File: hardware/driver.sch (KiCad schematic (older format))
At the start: 12 parts

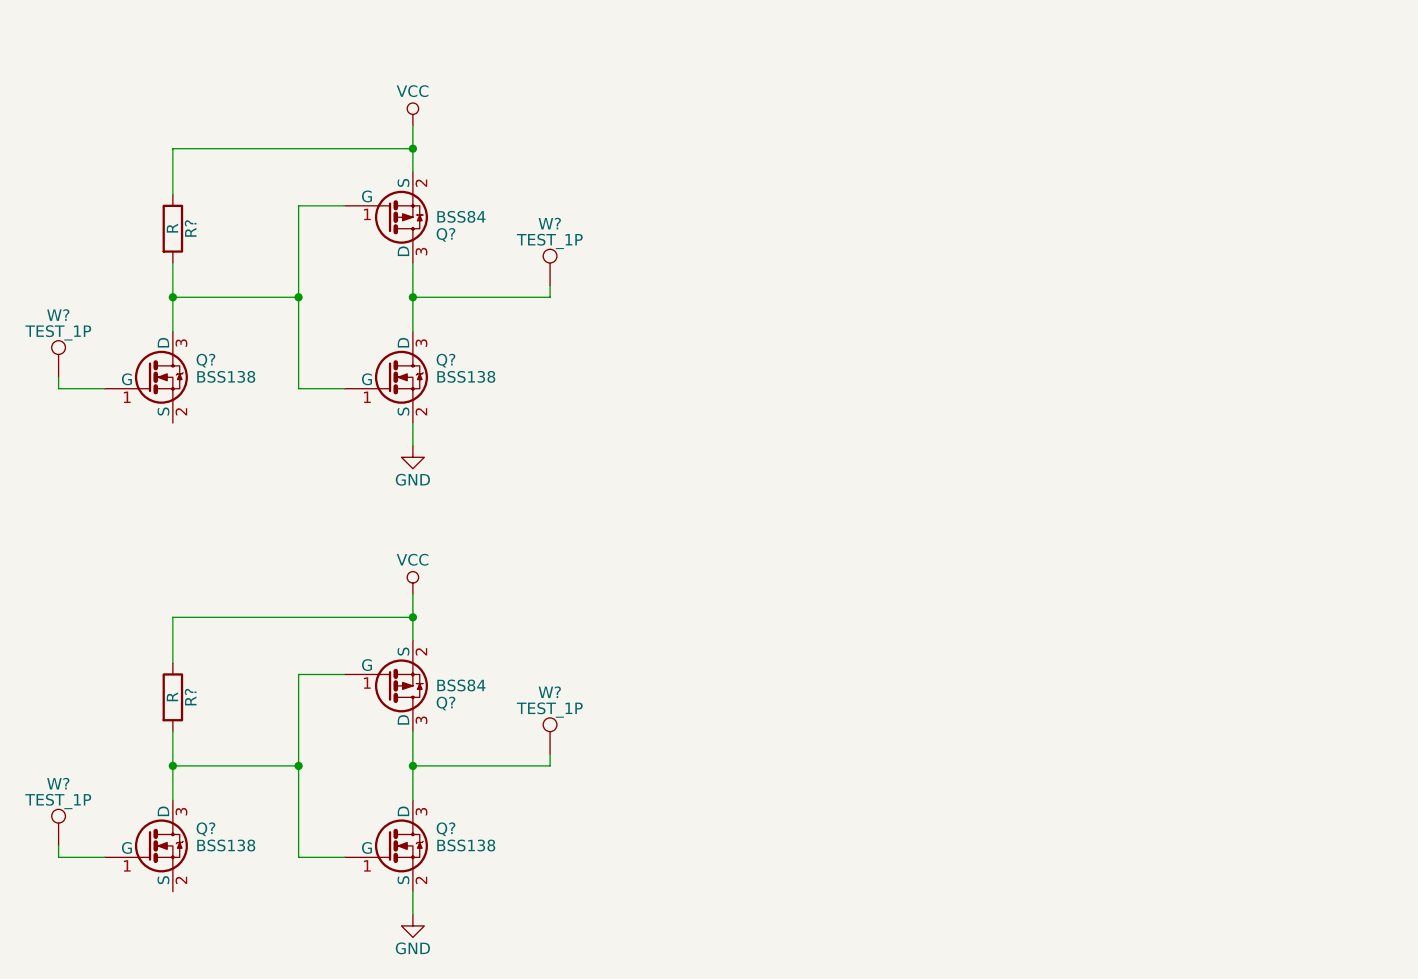
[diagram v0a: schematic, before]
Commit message: Fixed FET orientation
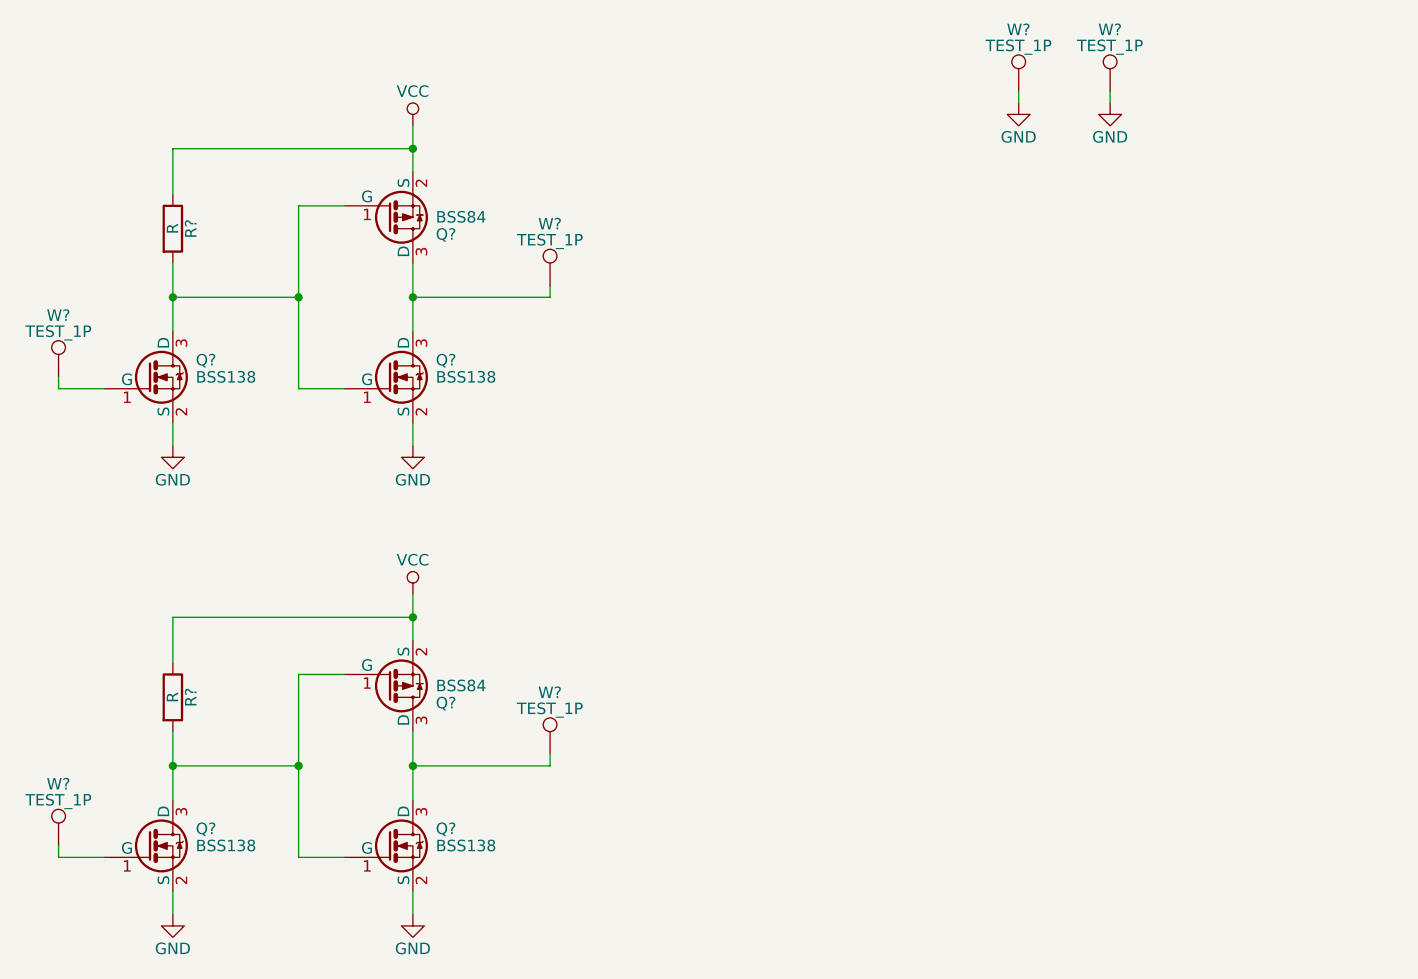
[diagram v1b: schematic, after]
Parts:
- added W? (x2): TEST_1P, symbol TEST_1P
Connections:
- net GND: now also Q?.2 (S), Q?.2 (S), W?.1, W?.1
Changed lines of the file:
@@
 	3500 3850 3500 4050
 Connection ~ 4550 3850
+$Comp
+L GND #PWR?
+U 1 1 5890FAB7
+P 3500 3100
+F 0 "#PWR?" H 3500 2850 50  0001 C CNN
+F 1 "GND" H 3500 2950 50  0000 C CNN
+F 2 "" H 3500 3100 50  0000 C CNN
+F 3 "" H 3500 3100 50  0000 C CNN
+	1    3500 3100
+	1    0    0    -1
+$EndComp
+Wire Wire Line
+	3500 3100 3500 3000
+$Comp
+L GND #PWR?
+U 1 1 5890FD28
+P 3500 5150
+F 0 "#PWR?" H 3500 4900 50  0001 C CNN
+F 1 "GND" H 3500 5000 50  0000 C CNN
+F 2 "" H 3500 5150 50  0000 C CNN
+F 3 "" H 3500 5150 50  0000 C CNN
+	1    3500 5150
+	1    0    0    -1
+$EndComp
+Wire Wire Line
+	3500 5150 3500 5050
+$Comp
+L TEST_1P W?
+U 1 1 58910040
+P 7200 1550
+F 0 "W?" H 7200 1820 50  0000 C CNN
+F 1 "TEST_1P" H 7200 1750 50  0000 C CNN
+F 2 "" H 7400 1550 50  0000 C CNN
+F 3 "" H 7400 1550 50  0000 C CNN
+	1    7200 1550
+	1    0    0    -1
+$EndComp
+$Comp
+L TEST_1P W?
+U 1 1 58910461
+P 7600 1550
+F 0 "W?" H 7600 1820 50  0000 C CNN
+F 1 "TEST_1P" H 7600 1750 50  0000 C CNN
+F 2 "" H 7800 1550 50  0000 C CNN
+F 3 "" H 7800 1550 50  0000 C CNN
+	1    7600 1550
+	1    0    0    -1
+$EndComp
+$Comp
+L GND #PWR?
+U 1 1 5891056F
+P 7200 1600
+F 0 "#PWR?" H 7200 1350 50  0001 C CNN
+F 1 "GND" H 7200 1450 50  0000 C CNN
+F 2 "" H 7200 1600 50  0000 C CNN
+F 3 "" H 7200 1600 50  0000 C CNN
+	1    7200 1600
+	1    0    0    -1
+$EndComp
+$Comp
+L GND #PWR?
+U 1 1 589105A4
+P 7600 1600
+F 0 "#PWR?" H 7600 1350 50  0001 C CNN
+F 1 "GND" H 7600 1450 50  0000 C CNN
+F 2 "" H 7600 1600 50  0000 C CNN
+F 3 "" H 7600 1600 50  0000 C CNN
+	1    7600 1600
+	1    0    0    -1
+$EndComp
+Wire Wire Line
+	7600 1600 7600 1550
+Wire Wire Line
+	7200 1550 7200 1600
 $EndSCHEMATC

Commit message: Added power flags
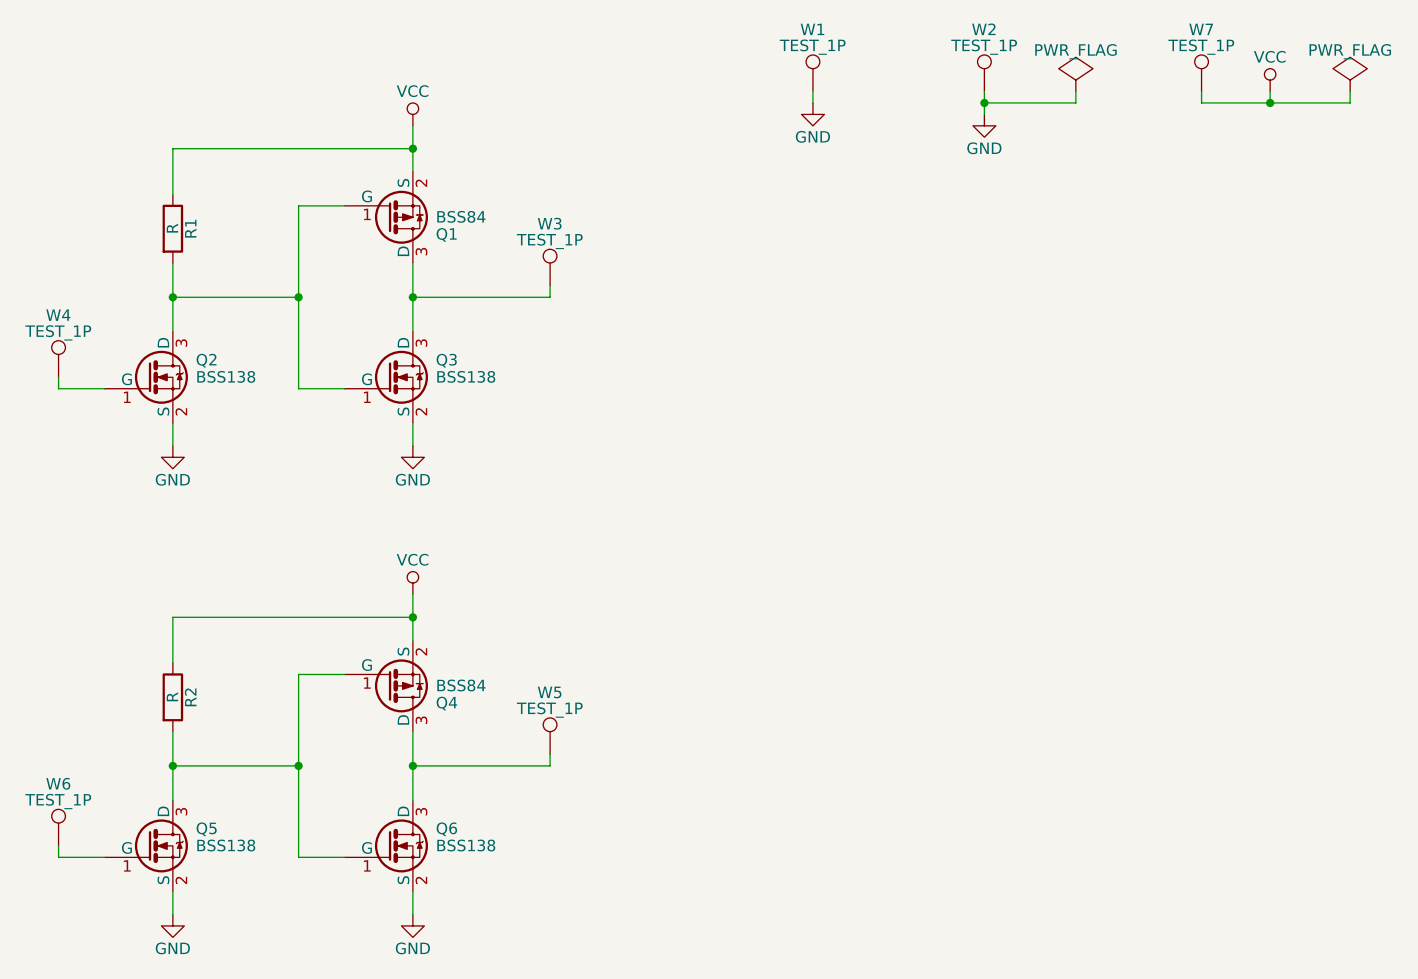
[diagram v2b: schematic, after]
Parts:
- added W7: TEST_1P, symbol TEST_1P
- gave numbers to parts that had none: 14
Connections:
- net VCC: now also W7.1
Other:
- moved on the sheet: W1, W2
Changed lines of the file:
@@
 $EndDescr
 $Comp
-L BSS84 Q?
+L BSS84 Q1
 U 1 1 588FBBAA
 P 4450 2100
-F 0 "Q?" H 4650 2175 50  0000 L CNN
+F 0 "Q1" H 4650 2175 50  0000 L CNN
 F 1 "BSS84" H 4650 2100 50  0000 L CNN
 F 2 "" H 4650 2025 50  0000 L CIN
@@
 $EndComp
 $Comp
-L BSS138 Q?
+L BSS138 Q2
 U 1 1 588FBC23
 P 3400 2800
-F 0 "Q?" H 3600 2875 50  0000 L CNN
+F 0 "Q2" H 3600 2875 50  0000 L CNN
 F 1 "BSS138" H 3600 2800 50  0000 L CNN
 F 2 "TO_SOT_Packages_SMD:SOT-23" H 3600 2725 50  0001 L CIN
@@
 $EndComp
 $Comp
-L GND #PWR?
+L GND #PWR01
 U 1 1 588FBD14
 P 4550 3100
-F 0 "#PWR?" H 4550 2850 50  0001 C CNN
+F 0 "#PWR01" H 4550 2850 50  0001 C CNN
 F 1 "GND" H 4550 2950 50  0000 C CNN
 F 2 "" H 4550 3100 50  0000 C CNN
@@
 $EndComp
 $Comp
-L VCC #PWR?
+L VCC #PWR02
 U 1 1 588FBD2C
 P 4550 1700
-F 0 "#PWR?" H 4550 1550 50  0001 C CNN
+F 0 "#PWR02" H 4550 1550 50  0001 C CNN
 F 1 "VCC" H 4550 1850 50  0000 C CNN
 F 2 "" H 4550 1700 50  0000 C CNN
@@
 $EndComp
 $Comp
-L R R?
+L R R1
 U 1 1 588FBD46
 P 3500 2150
-F 0 "R?" V 3580 2150 50  0000 C CNN
+F 0 "R1" V 3580 2150 50  0000 C CNN
 F 1 "R" V 3500 2150 50  0000 C CNN
 F 2 "" V 3430 2150 50  0000 C CNN
@@
 $EndComp
 $Comp
-L TEST_1P W?
+L TEST_1P W4
 U 1 1 588FBD89
 P 3000 2800
-F 0 "W?" H 3000 3070 50  0000 C CNN
+F 0 "W4" H 3000 3070 50  0000 C CNN
 F 1 "TEST_1P" H 3000 3000 50  0000 C CNN
 F 2 "" H 3200 2800 50  0000 C CNN
@@
 $EndComp
 $Comp
-L BSS138 Q?
+L BSS138 Q3
 U 1 1 588FC012
 P 4450 2800
-F 0 "Q?" H 4650 2875 50  0000 L CNN
+F 0 "Q3" H 4650 2875 50  0000 L CNN
 F 1 "BSS138" H 4650 2800 50  0000 L CNN
 F 2 "TO_SOT_Packages_SMD:SOT-23" H 4650 2725 50  0001 L CIN
@@
 	4550 3100 4550 3000
 $Comp
-L VCC #PWR?
+L VCC #PWR03
 U 1 1 588FC3B7
 P 4550 3750
-F 0 "#PWR?" H 4550 3600 50  0001 C CNN
+F 0 "#PWR03" H 4550 3600 50  0001 C CNN
 F 1 "VCC" H 4550 3900 50  0000 C CNN
 F 2 "" H 4550 3750 50  0000 C CNN
@@
 $EndComp
 $Comp
-L BSS84 Q?
+L BSS84 Q4
 U 1 1 588FC42B
 P 4450 4150
-F 0 "Q?" H 4650 4225 50  0000 L CNN
+F 0 "Q4" H 4650 4225 50  0000 L CNN
 F 1 "BSS84" H 4650 4150 50  0000 L CNN
 F 2 "" H 4650 4075 50  0000 L CIN
@@
 Connection ~ 4550 4500
 $Comp
-L BSS138 Q?
+L BSS138 Q6
 U 1 1 588FC62C
 P 4450 4850
-F 0 "Q?" H 4650 4925 50  0000 L CNN
+F 0 "Q6" H 4650 4925 50  0000 L CNN
 F 1 "BSS138" H 4650 4850 50  0000 L CNN
 F 2 "TO_SOT_Packages_SMD:SOT-23" H 4650 4775 50  0001 L CIN
@@
 $EndComp
 $Comp
-L GND #PWR?
+L GND #PWR04
 U 1 1 588FC66D
 P 4550 5150
-F 0 "#PWR?" H 4550 4900 50  0001 C CNN
+F 0 "#PWR04" H 4550 4900 50  0001 C CNN
 F 1 "GND" H 4550 5000 50  0000 C CNN
 F 2 "" H 4550 5150 50  0000 C CNN
@@
 Connection ~ 4050 4500
 $Comp
-L BSS138 Q?
+L BSS138 Q5
 U 1 1 588FC9C8
 P 3400 4850
-F 0 "Q?" H 3600 4925 50  0000 L CNN
+F 0 "Q5" H 3600 4925 50  0000 L CNN
 F 1 "BSS138" H 3600 4850 50  0000 L CNN
 F 2 "TO_SOT_Packages_SMD:SOT-23" H 3600 4775 50  0001 L CIN
@@
 Connection ~ 3500 4500
 $Comp
-L R R?
+L R R2
 U 1 1 588FCB0A
 P 3500 4200
-F 0 "R?" V 3580 4200 50  0000 C CNN
+F 0 "R2" V 3580 4200 50  0000 C CNN
 F 1 "R" V 3500 4200 50  0000 C CNN
 F 2 "" V 3430 4200 50  0000 C CNN
@@
 	3000 2850 3000 2800
 $Comp
-L TEST_1P W?
+L TEST_1P W6
 U 1 1 588FCDEE
 P 3000 4850
-F 0 "W?" H 3000 5120 50  0000 C CNN
+F 0 "W6" H 3000 5120 50  0000 C CNN
 F 1 "TEST_1P" H 3000 5050 50  0000 C CNN
 F 2 "" H 3200 4850 50  0000 C CNN
@@
 	3000 4900 3000 4850
 $Comp
-L TEST_1P W?
+L TEST_1P W5
 U 1 1 588FD19C
 P 5150 4450
-F 0 "W?" H 5150 4720 50  0000 C CNN
+F 0 "W5" H 5150 4720 50  0000 C CNN
 F 1 "TEST_1P" H 5150 4650 50  0000 C CNN
 F 2 "" H 5350 4450 50  0000 C CNN
@@
 $EndComp
 $Comp
-L TEST_1P W?
+L TEST_1P W3
 U 1 1 588FD262
 P 5150 2400
-F 0 "W?" H 5150 2670 50  0000 C CNN
+F 0 "W3" H 5150 2670 50  0000 C CNN
 F 1 "TEST_1P" H 5150 2600 50  0000 C CNN
 F 2 "" H 5350 2400 50  0000 C CNN
@@
 Connection ~ 4550 3850
 $Comp
-L GND #PWR?
+L GND #PWR05
 U 1 1 5890FAB7
 P 3500 3100
-F 0 "#PWR?" H 3500 2850 50  0001 C CNN
+F 0 "#PWR05" H 3500 2850 50  0001 C CNN
 F 1 "GND" H 3500 2950 50  0000 C CNN
 F 2 "" H 3500 3100 50  0000 C CNN
@@
 	3500 3100 3500 3000
 $Comp
-L GND #PWR?
+L GND #PWR06
 U 1 1 5890FD28
 P 3500 5150
-F 0 "#PWR?" H 3500 4900 50  0001 C CNN
+F 0 "#PWR06" H 3500 4900 50  0001 C CNN
 F 1 "GND" H 3500 5000 50  0000 C CNN
 F 2 "" H 3500 5150 50  0000 C CNN
@@
 	3500 5150 3500 5050
 $Comp
-L TEST_1P W?
+L TEST_1P W1
 U 1 1 58910040
-P 7200 1550
-F 0 "W?" H 7200 1820 50  0000 C CNN
-F 1 "TEST_1P" H 7200 1750 50  0000 C CNN
-F 2 "" H 7400 1550 50  0000 C CNN
-F 3 "" H 7400 1550 50  0000 C CNN
-	1    7200 1550
-	1    0    0    -1
-$EndComp
-$Comp
-L TEST_1P W?
+P 6300 1550
+F 0 "W1" H 6300 1820 50  0000 C CNN
+F 1 "TEST_1P" H 6300 1750 50  0000 C CNN
+F 2 "" H 6500 1550 50  0000 C CNN
+F 3 "" H 6500 1550 50  0000 C CNN
+	1    6300 1550
+	1    0    0    -1
+$EndComp
+$Comp
+L TEST_1P W2
 U 1 1 58910461
-P 7600 1550
-F 0 "W?" H 7600 1820 50  0000 C CNN
-F 1 "TEST_1P" H 7600 1750 50  0000 C CNN
-F 2 "" H 7800 1550 50  0000 C CNN
-F 3 "" H 7800 1550 50  0000 C CNN
-	1    7600 1550
-	1    0    0    -1
-$EndComp
-$Comp
-L GND #PWR?
+P 7050 1550
+F 0 "W2" H 7050 1820 50  0000 C CNN
+F 1 "TEST_1P" H 7050 1750 50  0000 C CNN
+F 2 "" H 7250 1550 50  0000 C CNN
+F 3 "" H 7250 1550 50  0000 C CNN
+	1    7050 1550
+	1    0    0    -1
+$EndComp
+$Comp
+L GND #PWR07
 U 1 1 5891056F
-P 7200 1600
-F 0 "#PWR?" H 7200 1350 50  0001 C CNN
-F 1 "GND" H 7200 1450 50  0000 C CNN
-F 2 "" H 7200 1600 50  0000 C CNN
-F 3 "" H 7200 1600 50  0000 C CNN
-	1    7200 1600
-	1    0    0    -1
-$EndComp
-$Comp
-L GND #PWR?
+P 6300 1600
+F 0 "#PWR07" H 6300 1350 50  0001 C CNN
+F 1 "GND" H 6300 1450 50  0000 C CNN
+F 2 "" H 6300 1600 50  0000 C CNN
+F 3 "" H 6300 1600 50  0000 C CNN
+	1    6300 1600
+	1    0    0    -1
+$EndComp
+$Comp
+L GND #PWR08
 U 1 1 589105A4
-P 7600 1600
-F 0 "#PWR?" H 7600 1350 50  0001 C CNN
-F 1 "GND" H 7600 1450 50  0000 C CNN
-F 2 "" H 7600 1600 50  0000 C CNN
-F 3 "" H 7600 1600 50  0000 C CNN
-	1    7600 1600
-	1    0    0    -1
-$EndComp
-Wire Wire Line
-	7600 1600 7600 1550
-Wire Wire Line
-	7200 1550 7200 1600
+P 7050 1650
+F 0 "#PWR08" H 7050 1400 50  0001 C CNN
+F 1 "GND" H 7050 1500 50  0000 C CNN
+F 2 "" H 7050 1650 50  0000 C CNN
+F 3 "" H 7050 1650 50  0000 C CNN
+	1    7050 1650
+	1    0    0    -1
+$EndComp
+Wire Wire Line
+	7050 1550 7050 1650
+Wire Wire Line
+	6300 1550 6300 1600
+$Comp
+L TEST_1P W7
+U 1 1 58922E12
+P 8000 1550
+F 0 "W7" H 8000 1820 50  0000 C CNN
+F 1 "TEST_1P" H 8000 1750 50  0000 C CNN
+F 2 "" H 8200 1550 50  0000 C CNN
+F 3 "" H 8200 1550 50  0000 C CNN
+	1    8000 1550
+	1    0    0    -1
+$EndComp
+$Comp
+L VCC #PWR09
+U 1 1 58922E63
+P 8300 1550
+F 0 "#PWR09" H 8300 1400 50  0001 C CNN
+F 1 "VCC" H 8300 1700 50  0000 C CNN
+F 2 "" H 8300 1550 50  0000 C CNN
+F 3 "" H 8300 1550 50  0000 C CNN
+	1    8300 1550
+	1    0    0    -1
+$EndComp
+Wire Wire Line
+	8000 1550 8000 1600
+Wire Wire Line
+	8000 1600 8650 1600
+Wire Wire Line
+	8300 1600 8300 1550
+$Comp
+L PWR_FLAG #FLG010
+U 1 1 5892349D
+P 8650 1550
+F 0 "#FLG010" H 8650 1645 50  0001 C CNN
+F 1 "PWR_FLAG" H 8650 1730 50  0000 C CNN
+F 2 "" H 8650 1550 50  0000 C CNN
+F 3 "" H 8650 1550 50  0000 C CNN
+	1    8650 1550
+	1    0    0    -1
+$EndComp
+Wire Wire Line
+	8650 1600 8650 1550
+Connection ~ 8300 1600
+$Comp
+L PWR_FLAG #FLG011
+U 1 1 589242AB
+P 7450 1550
+F 0 "#FLG011" H 7450 1645 50  0001 C CNN
+F 1 "PWR_FLAG" H 7450 1730 50  0000 C CNN
+F 2 "" H 7450 1550 50  0000 C CNN
+F 3 "" H 7450 1550 50  0000 C CNN
+	1    7450 1550
+	1    0    0    -1
+$EndComp
+Wire Wire Line
+	7050 1600 7450 1600
+Wire Wire Line
+	7450 1600 7450 1550
+Connection ~ 7050 1600
 $EndSCHEMATC

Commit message: Names/annotation
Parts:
- W2: value TEST_1P -> GND
- W3: value TEST_1P -> OUT1
- W4: value TEST_1P -> IN1
- W5: value TEST_1P -> OUT2
- W6: value TEST_1P -> IN2
- W7: value TEST_1P -> VCC
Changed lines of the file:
@@
 encoding utf-8
 Sheet 1 1
-Title ""
-Date ""
-Rev ""
-Comp ""
+Title "FET push-pull driver"
+Date "2017-02-01"
+Rev "1.0"
+Comp "KEIO"
 Comment1 ""
 Comment2 ""
@@
 P 3000 2800
 F 0 "W4" H 3000 3070 50  0000 C CNN
-F 1 "TEST_1P" H 3000 3000 50  0000 C CNN
+F 1 "IN1" H 3000 3000 50  0000 C CNN
 F 2 "" H 3200 2800 50  0000 C CNN
 F 3 "" H 3200 2800 50  0000 C CNN
@@
 P 3000 4850
 F 0 "W6" H 3000 5120 50  0000 C CNN
-F 1 "TEST_1P" H 3000 5050 50  0000 C CNN
+F 1 "IN2" H 3000 5050 50  0000 C CNN
 F 2 "" H 3200 4850 50  0000 C CNN
 F 3 "" H 3200 4850 50  0000 C CNN
@@
 P 5150 4450
 F 0 "W5" H 5150 4720 50  0000 C CNN
-F 1 "TEST_1P" H 5150 4650 50  0000 C CNN
+F 1 "OUT2" H 5150 4650 50  0000 C CNN
 F 2 "" H 5350 4450 50  0000 C CNN
 F 3 "" H 5350 4450 50  0000 C CNN
@@
 P 5150 2400
 F 0 "W3" H 5150 2670 50  0000 C CNN
-F 1 "TEST_1P" H 5150 2600 50  0000 C CNN
+F 1 "OUT1" H 5150 2600 50  0000 C CNN
 F 2 "" H 5350 2400 50  0000 C CNN
 F 3 "" H 5350 2400 50  0000 C CNN
@@
 P 7050 1550
 F 0 "W2" H 7050 1820 50  0000 C CNN
-F 1 "TEST_1P" H 7050 1750 50  0000 C CNN
+F 1 "GND" H 7050 1750 50  0000 C CNN
 F 2 "" H 7250 1550 50  0000 C CNN
 F 3 "" H 7250 1550 50  0000 C CNN
@@
 P 8000 1550
 F 0 "W7" H 8000 1820 50  0000 C CNN
-F 1 "TEST_1P" H 8000 1750 50  0000 C CNN
+F 1 "VCC" H 8000 1750 50  0000 C CNN
 F 2 "" H 8200 1550 50  0000 C CNN
 F 3 "" H 8200 1550 50  0000 C CNN
